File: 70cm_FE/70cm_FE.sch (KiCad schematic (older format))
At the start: 150 parts, among them J2 U.FL, J3 U.FL, J4 U.FL, Q1 2SC3356, Q2 2SC3356, Q3 2SC3356, Q4 2N7002, U1 HT7533-1, U2 74HC14, U3 74HC14, U4 LM393, U5 M68710L

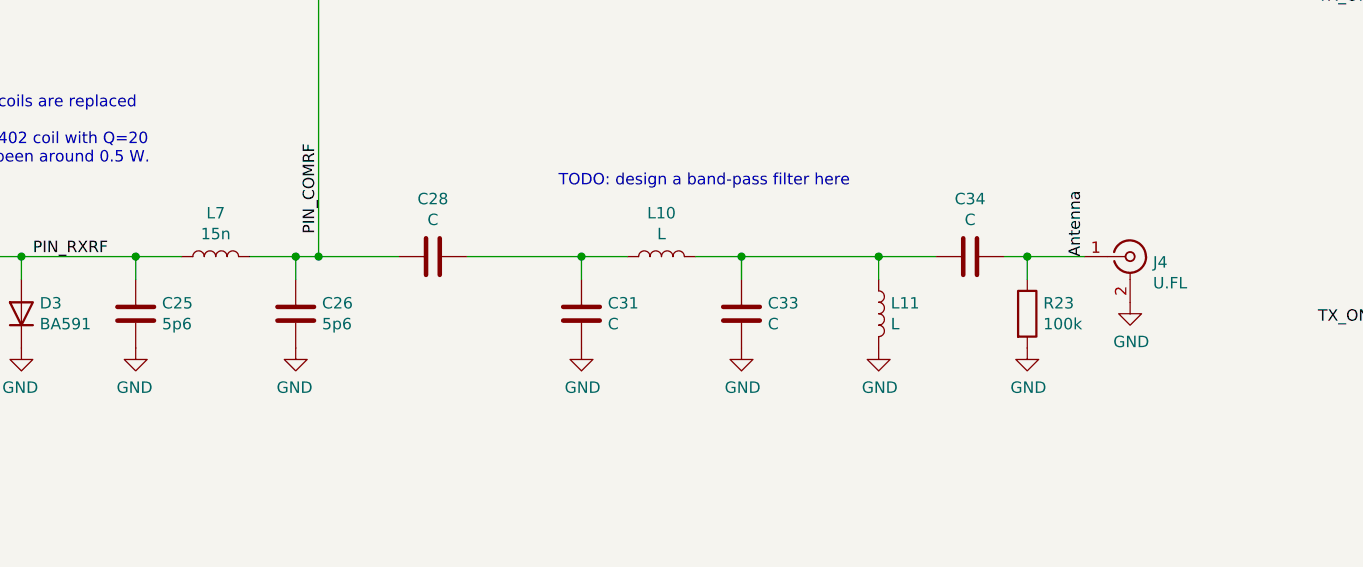
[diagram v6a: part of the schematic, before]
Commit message: Change PCB size to 50x70 mm, place some components
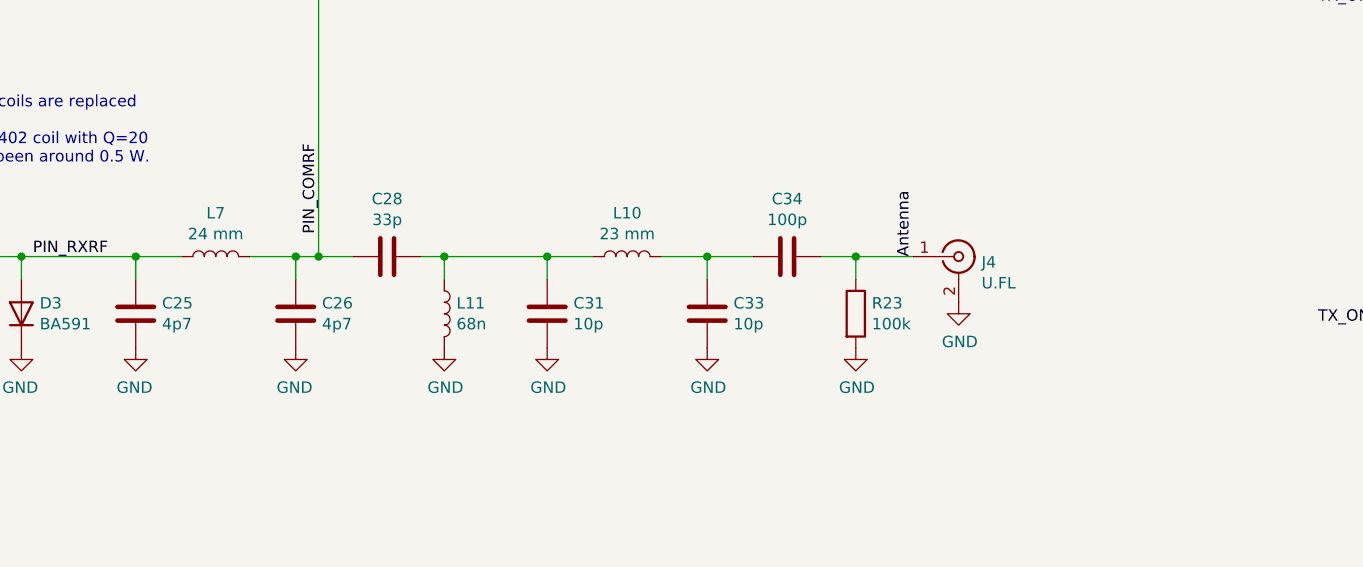
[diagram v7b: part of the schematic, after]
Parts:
- C25, C26: value 5p6 -> 4p7
- C28: value C -> 33p
- C31, C33: value C -> 10p
- C34: value C -> 100p
- L10: value L -> 23 mm; footprint 70cm_FE:NetTie-2_SMD_Pad0.2mm -> 70cm_FE:NetTie-2_SMD_Pad0.25mm
- L11: value L -> 68n
- L7: value 15n -> 24 mm; footprint 70cm_FE:NetTie-2_SMD_Pad0.2mm -> 70cm_FE:NetTie-2_SMD_Pad0.25mm
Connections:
- net at C28.2, C31.1, L10.1: now also L11.1
- net at C33.1, C34.1, L10.2: no longer L11.1
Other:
- note removed: "TODO: design a band-pass filter here"
- moved on the sheet: C28, C31, C33, C34, J4, L10, L11, R23
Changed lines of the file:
@@
 L Device:L L11
 U 1 1 5F9292DD
-P 10800 8500
-F 0 "L11" H 10853 8546 50  0000 L CNN
-F 1 "L" H 10853 8455 50  0000 L CNN
-F 2 "Inductor_SMD:L_0603_1608Metric" H 10800 8500 50  0001 C CNN
-F 3 "~" H 10800 8500 50  0001 C CNN
-	1    10800 8500
+P 8900 8500
+F 0 "L11" H 8953 8546 50  0000 L CNN
+F 1 "68n" H 8953 8455 50  0000 L CNN
+F 2 "Inductor_SMD:L_0603_1608Metric" H 8900 8500 50  0001 C CNN
+F 3 "~" H 8900 8500 50  0001 C CNN
+	1    8900 8500
 	1    0    0    -1
 $EndComp
@@
 L power:GND #PWR049
 U 1 1 5F9298DC
-P 10800 8650
-F 0 "#PWR049" H 10800 8400 50  0001 C CNN
-F 1 "GND" H 10805 8477 50  0000 C CNN
-F 2 "" H 10800 8650 50  0001 C CNN
-F 3 "" H 10800 8650 50  0001 C CNN
-	1    10800 8650
+P 8900 8650
+F 0 "#PWR049" H 8900 8400 50  0001 C CNN
+F 1 "GND" H 8905 8477 50  0000 C CNN
+F 2 "" H 8900 8650 50  0001 C CNN
+F 3 "" H 8900 8650 50  0001 C CNN
+	1    8900 8650
 	1    0    0    -1
 $EndComp
 Wire Wire Line
-	10800 8350 10800 8250
+	8900 8350 8900 8250
 $Comp
 L Device:C C34
 U 1 1 5F92A2BD
-P 11200 8250
-F 0 "C34" V 11452 8250 50  0000 C CNN
-F 1 "C" V 11361 8250 50  0000 C CNN
-F 2 "Capacitor_SMD:C_0603_1608Metric" H 11238 8100 50  0001 C CNN
-F 3 "~" H 11200 8250 50  0001 C CNN
-	1    11200 8250
+P 10400 8250
+F 0 "C34" V 10652 8250 50  0000 C CNN
+F 1 "100p" V 10561 8250 50  0000 C CNN
+F 2 "Capacitor_SMD:C_0603_1608Metric" H 10438 8100 50  0001 C CNN
+F 3 "~" H 10400 8250 50  0001 C CNN
+	1    10400 8250
 	0    -1   -1   0
 $EndComp
 Wire Wire Line
-	11050 8250 10800 8250
-Wire Wire Line
-	11450 8350 11450 8250
-Wire Wire Line
-	11450 8250 11350 8250
+	10700 8350 10700 8250
 $Comp
 L power:GND #PWR050
 U 1 1 5F92C034
-P 11450 8650
-F 0 "#PWR050" H 11450 8400 50  0001 C CNN
-F 1 "GND" H 11455 8477 50  0000 C CNN
-F 2 "" H 11450 8650 50  0001 C CNN
-F 3 "" H 11450 8650 50  0001 C CNN
-	1    11450 8650
+P 10700 8650
+F 0 "#PWR050" H 10700 8400 50  0001 C CNN
+F 1 "GND" H 10705 8477 50  0000 C CNN
+F 2 "" H 10700 8650 50  0001 C CNN
+F 3 "" H 10700 8650 50  0001 C CNN
+	1    10700 8650
 	1    0    0    -1
 $EndComp
@@
 L Connector:Conn_Coaxial J4
 U 1 1 5FA39C30
-P 11900 8250
-F 0 "J4" H 12000 8225 50  0000 L CNN
-F 1 "U.FL" H 12000 8134 50  0000 L CNN
-F 2 "Connector_Coaxial:U.FL_Hirose_U.FL-R-SMT-1_Vertical" H 11900 8250 50  0001 C CNN
-F 3 " ~" H 11900 8250 50  0001 C CNN
-	1    11900 8250
+P 11150 8250
+F 0 "J4" H 11250 8225 50  0000 L CNN
+F 1 "U.FL" H 11250 8134 50  0000 L CNN
+F 2 "Connector_Coaxial:U.FL_Hirose_U.FL-R-SMT-1_Vertical" H 11150 8250 50  0001 C CNN
+F 3 " ~" H 11150 8250 50  0001 C CNN
+	1    11150 8250
 	1    0    0    -1
 $EndComp
@@
 L power:GND #PWR053
 U 1 1 5FA3C65A
-P 11900 8450
-F 0 "#PWR053" H 11900 8200 50  0001 C CNN
-F 1 "GND" H 11905 8277 50  0000 C CNN
-F 2 "" H 11900 8450 50  0001 C CNN
-F 3 "" H 11900 8450 50  0001 C CNN
-	1    11900 8450
+P 11150 8450
+F 0 "#PWR053" H 11150 8200 50  0001 C CNN
+F 1 "GND" H 11155 8277 50  0000 C CNN
+F 2 "" H 11150 8450 50  0001 C CNN
+F 3 "" H 11150 8450 50  0001 C CNN
+	1    11150 8450
 	1    0    0    -1
 $EndComp
 Wire Wire Line
-	11700 8250 11450 8250
-Connection ~ 11450 8250
+	10950 8250 10700 8250
 $Comp
 L Device:C C2
@@
 	2550 850  2100 850
 Connection ~ 2100 850
-Text Label 11700 8250 1    50   ~ 0
+Text Label 10950 8250 1    50   ~ 0
 Antenna
 $Comp
@@
 L Device:R R23
 U 1 1 5F92B686
-P 11450 8500
-F 0 "R23" H 11520 8546 50  0000 L CNN
-F 1 "100k" H 11520 8455 50  0000 L CNN
-F 2 "Resistor_SMD:R_0402_1005Metric" V 11380 8500 50  0001 C CNN
-F 3 "~" H 11450 8500 50  0001 C CNN
-	1    11450 8500
+P 10700 8500
+F 0 "R23" H 10770 8546 50  0000 L CNN
+F 1 "100k" H 10770 8455 50  0000 L CNN
+F 2 "Resistor_SMD:R_0402_1005Metric" V 10630 8500 50  0001 C CNN
+F 3 "~" H 10700 8500 50  0001 C CNN
+	1    10700 8500
 	1    0    0    -1
 $EndComp
@@
 Text Label 14300 2450 0    50   ~ 0
 ~OverTemp~
-Connection ~ 10800 8250
-Text Notes 9400 7950 0    50   ~ 0
-TODO: design a band-pass filter here
 Text Label 8350 8150 1    50   ~ 0
 PIN_COMRF
@@
 	7050 8250 6900 8250
 Wire Wire Line
-	8350 8250 8700 8250
+	8350 8250 8500 8250
 Connection ~ 8350 8250
 Wire Wire Line
@@
 	-1   0    0    -1
 $EndComp
-Connection ~ 10200 8250
-Wire Wire Line
-	10800 8250 10200 8250
+Connection ~ 10050 8250
 $Comp
 L power:GND #PWR048
 U 1 1 5F925DFF
-P 10200 8650
-F 0 "#PWR048" H 10200 8400 50  0001 C CNN
-F 1 "GND" H 10205 8477 50  0000 C CNN
-F 2 "" H 10200 8650 50  0001 C CNN
-F 3 "" H 10200 8650 50  0001 C CNN
-	1    10200 8650
+P 10050 8650
+F 0 "#PWR048" H 10050 8400 50  0001 C CNN
+F 1 "GND" H 10055 8477 50  0000 C CNN
+F 2 "" H 10050 8650 50  0001 C CNN
+F 3 "" H 10050 8650 50  0001 C CNN
+	1    10050 8650
 	1    0    0    -1
 $EndComp
 Wire Wire Line
-	10200 8250 10000 8250
+	10050 8250 9850 8250
 Wire Wire Line
-	10200 8350 10200 8250
+	10050 8350 10050 8250
 $Comp
 L Device:C C33
 U 1 1 5F925DF3
-P 10200 8500
-F 0 "C33" H 10315 8546 50  0000 L CNN
-F 1 "C" H 10315 8455 50  0000 L CNN
-F 2 "Capacitor_SMD:C_0603_1608Metric" H 10238 8350 50  0001 C CNN
-F 3 "~" H 10200 8500 50  0001 C CNN
-	1    10200 8500
+P 10050 8500
+F 0 "C33" H 10165 8546 50  0000 L CNN
+F 1 "10p" H 10165 8455 50  0000 L CNN
+F 2 "Capacitor_SMD:C_0603_1608Metric" H 10088 8350 50  0001 C CNN
+F 3 "~" H 10050 8500 50  0001 C CNN
+	1    10050 8500
 	1    0    0    -1
 $EndComp
-Connection ~ 9500 8250
 Wire Wire Line
-	9700 8250 9500 8250
+	9550 8250 9350 8250
 $Comp
 L Device:L L10
 U 1 1 5F925DE7
-P 9850 8250
-F 0 "L10" V 10040 8250 50  0000 C CNN
-F 1 "L" V 9949 8250 50  0000 C CNN
-F 2 "70cm_FE:NetTie-2_SMD_Pad0.2mm" H 9850 8250 50  0001 C CNN
-F 3 "~" H 9850 8250 50  0001 C CNN
-	1    9850 8250
+P 9700 8250
+F 0 "L10" V 9890 8250 50  0000 C CNN
+F 1 "23 mm" V 9799 8250 50  0000 C CNN
+F 2 "70cm_FE:NetTie-2_SMD_Pad0.25mm" H 9700 8250 50  0001 C CNN
+F 3 "~" H 9700 8250 50  0001 C CNN
+	1    9700 8250
 	0    -1   -1   0
 $EndComp
@@
 L power:GND #PWR047
 U 1 1 5F925DDD
-P 9500 8650
-F 0 "#PWR047" H 9500 8400 50  0001 C CNN
-F 1 "GND" H 9505 8477 50  0000 C CNN
-F 2 "" H 9500 8650 50  0001 C CNN
-F 3 "" H 9500 8650 50  0001 C CNN
-	1    9500 8650
+P 9350 8650
+F 0 "#PWR047" H 9350 8400 50  0001 C CNN
+F 1 "GND" H 9355 8477 50  0000 C CNN
+F 2 "" H 9350 8650 50  0001 C CNN
+F 3 "" H 9350 8650 50  0001 C CNN
+	1    9350 8650
 	1    0    0    -1
 $EndComp
 Wire Wire Line
-	9500 8250 9000 8250
-Wire Wire Line
-	9500 8350 9500 8250
+	9350 8350 9350 8250
 $Comp
 L Device:C C31
 U 1 1 5F925DD1
-P 9500 8500
-F 0 "C31" H 9615 8546 50  0000 L CNN
-F 1 "C" H 9615 8455 50  0000 L CNN
-F 2 "Capacitor_SMD:C_0603_1608Metric" H 9538 8350 50  0001 C CNN
-F 3 "~" H 9500 8500 50  0001 C CNN
-	1    9500 8500
+P 9350 8500
+F 0 "C31" H 9465 8546 50  0000 L CNN
+F 1 "10p" H 9465 8455 50  0000 L CNN
+F 2 "Capacitor_SMD:C_0603_1608Metric" H 9388 8350 50  0001 C CNN
+F 3 "~" H 9350 8500 50  0001 C CNN
+	1    9350 8500
 	1    0    0    -1
 $EndComp
@@
 L Device:C C28
 U 1 1 5F9117D0
-P 8850 8250
-F 0 "C28" V 9102 8250 50  0000 C CNN
-F 1 "C" V 9011 8250 50  0000 C CNN
-F 2 "Capacitor_SMD:C_0603_1608Metric" H 8888 8100 50  0001 C CNN
-F 3 "~" H 8850 8250 50  0001 C CNN
-	1    8850 8250
+P 8650 8250
+F 0 "C28" V 8902 8250 50  0000 C CNN
+F 1 "33p" V 8811 8250 50  0000 C CNN
+F 2 "Capacitor_SMD:C_0603_1608Metric" H 8688 8100 50  0001 C CNN
+F 3 "~" H 8650 8250 50  0001 C CNN
+	1    8650 8250
 	0    -1   -1   0
 $EndComp
@@
 P 7550 8500
 F 0 "C25" H 7665 8546 50  0000 L CNN
-F 1 "5p6" H 7665 8455 50  0000 L CNN
+F 1 "4p7" H 7665 8455 50  0000 L CNN
 F 2 "Capacitor_SMD:C_0603_1608Metric" H 7588 8350 50  0001 C CNN
 F 3 "~" H 7550 8500 50  0001 C CNN
@@
 P 7900 8250
 F 0 "L7" V 8090 8250 50  0000 C CNN
-F 1 "15n" V 7999 8250 50  0000 C CNN
-F 2 "70cm_FE:NetTie-2_SMD_Pad0.2mm" H 7900 8250 50  0001 C CNN
+F 1 "24 mm" V 7999 8250 50  0000 C CNN
+F 2 "70cm_FE:NetTie-2_SMD_Pad0.25mm" H 7900 8250 50  0001 C CNN
 F 3 "~" H 7900 8250 50  0001 C CNN
 	1    7900 8250
@@
 P 8250 8500
 F 0 "C26" H 8365 8546 50  0000 L CNN
-F 1 "5p6" H 8365 8455 50  0000 L CNN
+F 1 "4p7" H 8365 8455 50  0000 L CNN
 F 2 "Capacitor_SMD:C_0603_1608Metric" H 8288 8350 50  0001 C CNN
 F 3 "~" H 8250 8500 50  0001 C CNN
@@
 Text Label 8300 1200 0    50   ~ 0
 TX_LED
+Wire Wire Line
+	10050 8250 10250 8250
+Wire Wire Line
+	8900 8250 8800 8250
+Wire Wire Line
+	9350 8250 8900 8250
+Connection ~ 9350 8250
+Connection ~ 8900 8250
+Wire Wire Line
+	10700 8250 10550 8250
+Connection ~ 10700 8250
 $EndSCHEMATC
